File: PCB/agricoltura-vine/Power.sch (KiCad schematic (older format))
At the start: 20 parts, among them T16 1757242, U4 AP63203WU-7, U5 AP63205WU-7

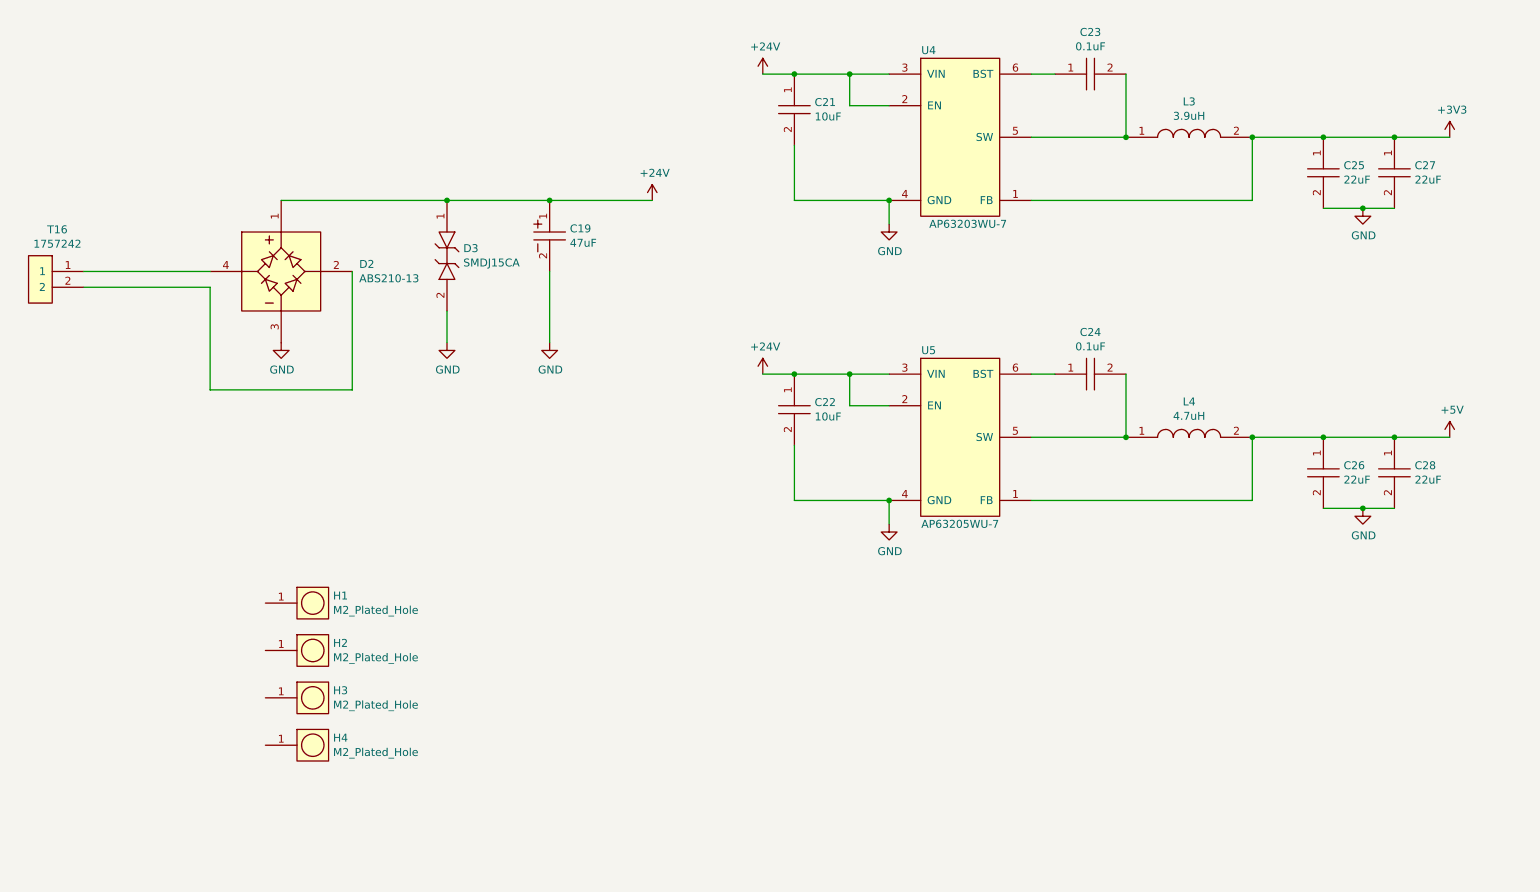
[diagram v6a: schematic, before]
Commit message: Routing and New RS485
swapped over the RS485 chip to a new one and started routing the board.
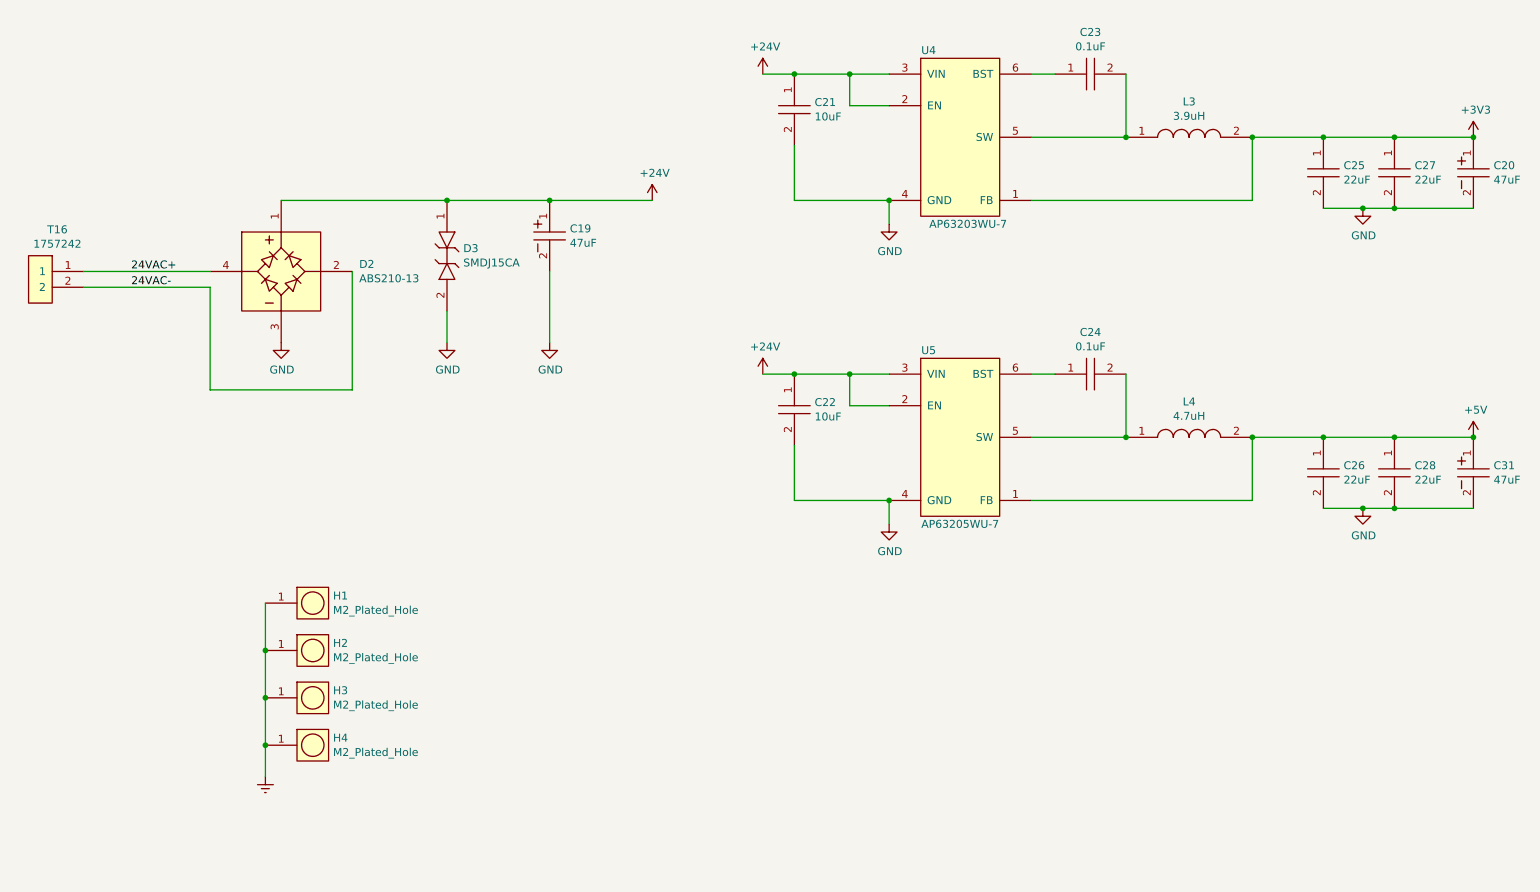
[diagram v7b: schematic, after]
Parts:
- added C20, C31: UCM1C470MCL1GS, AVR-KiCAD-Lib-Capacitors:UCM1C470MCL1GS, symbol AVR-KiCAD-Lib-Capacitors:UCM1C470MCL1GS
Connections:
- net +3V3: now also C20.1
- net +5V: now also C31.1
- net GND: now also C20.2, C31.2
- net 24VAC-: now reaches D2.2, T16.2
- net 24VAC+: now reaches D2.4, T16.1
- net Earth: now reaches H1.1
- net Earth: now also H2.1, H3.1, H4.1

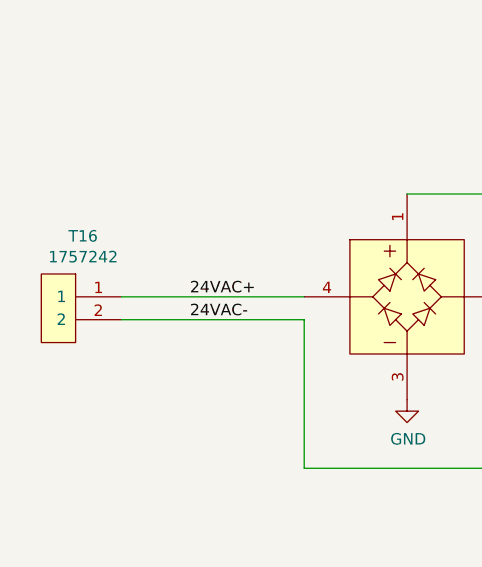
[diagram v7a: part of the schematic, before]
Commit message: IO Expander
added IO expander for 5V IOs
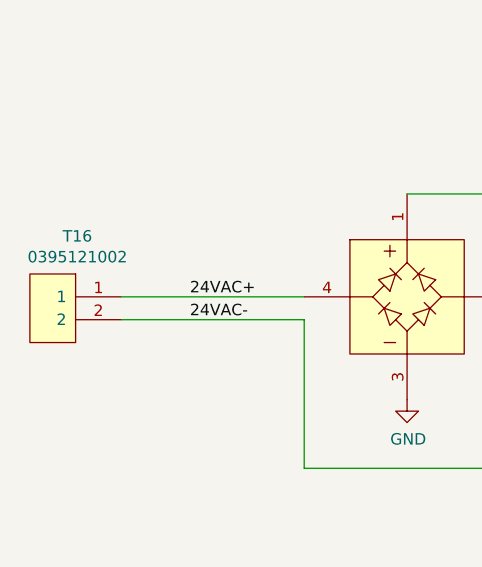
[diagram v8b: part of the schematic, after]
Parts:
- removed T16: 1757242, AVR-KiCAD-Lib-Connectors:PhoenixContact_MSTBA-G_02x5.08mm_Angled, symbol AVR-KiCAD-Lib-Connectors:1757242
- added T16: 0395121002, AVR-KiCAD-Lib-Connectors:0395121002, symbol AVR-KiCAD-Lib-Connectors:0395121002
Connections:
- net 24VAC+: now also T16.1
- net 24VAC-: now also T16.2
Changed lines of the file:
@@
 	1    0    0    -1
-$EndComp
-$Comp
-L AVR-KiCAD-Lib-Connectors:1757242 T16
-U 1 1 5EF359F8
-P 1200 3300
-F 0 "T16" H 1167 3365 50  0000 C CNN
-F 1 "1757242" H 1167 3274 50  0000 C CNN
-F 2 "AVR-KiCAD-Lib-Connectors:PhoenixContact_MSTBA-G_02x5.08mm_Angled" H 1000 3300 50  0001 C CNN
-F 3 "https://media.digikey.com/pdf/Data%20Sheets/Phoenix%20Contact%20PDFs/1757242.pdf" H 1100 3400 50  0001 C CNN
-F 4 "0.64000" H 1300 3550 50  0001 C CNN "Cost QTY: 1"
-F 5 "0.45518" H 1400 3650 50  0001 C CNN "Cost QTY: 1000"
-F 6 "0.43375" H 1500 3750 50  0001 C CNN "Cost QTY: 2500"
-F 7 "0.40698" H 1600 3850 50  0001 C CNN "Cost QTY: 5000"
-F 8 "*" H 1700 3950 50  0001 C CNN "Cost QTY: 10000"
-F 9 "Phoenix Contact" H 1800 4050 50  0001 C CNN "MFR"
-F 10 "1757242" H 1900 4150 50  0001 C CNN "MFR#"
-F 11 "Digikey" H 2000 4250 50  0001 C CNN "Vendor"
-F 12 "277-1106-ND" H 2100 4350 50  0001 C CNN "Vendor #"
-F 13 "AVR" H 2200 4450 50  0001 C CNN "Designer"
-F 14 "12mm" H 2300 4550 50  0001 C CNN "Height"
-F 15 "6/20/2020" H 3400 5650 50  0001 C CNN "Date Created"
-F 16 "6/20/2020" H 2400 4650 50  0001 C CNN "Date Modified"
-F 17 "Yes" H 2500 4750 50  0001 C CNN "Lead-Free ?"
-F 18 "1" H 2600 4850 50  0001 C CNN "RoHS Levels"
-F 19 "ThroughHole" H 2700 4950 50  0001 C CNN "Mounting"
-F 20 "2" H 2800 5050 50  0001 C CNN "Pin Count #"
-F 21 "Active" H 2900 5150 50  0001 C CNN "Status"
-F 22 "*" H 3000 5250 50  0001 C CNN "Tolerance"
-F 23 "Connector" H 3100 5350 50  0001 C CNN "Type"
-F 24 "300V" H 3200 5450 50  0001 C CNN "Voltage"
-F 25 "*" H 3300 5600 50  0001 C CNN "Package"
-F 26 "2 Position Terminal Block Header, Male Pins, Shrouded (4 Side) 0.200\" (5.08mm) 90°, Right Angle  Through Hole" H 3700 6000 50  0001 C CNN "Description"
-F 27 "1757242" H 3500 5800 50  0001 C CNN "_Value_"
-F 28 "*" H 3600 5900 50  0001 C CNN "Management_ID"
-	1    1200 3300
-	-1   0    0    -1
 $EndComp
 Wire Wire Line
@@
 	9700 3100 10200 3100
 Connection ~ 9700 3100
+$Comp
+L AVR-KiCAD-Lib-Connectors:0395121002 T16
+U 1 1 5F06CA83
+P 1200 3500
+F 0 "T16" H 1192 3765 50  0000 C CNN
+F 1 "0395121002" H 1192 3674 50  0000 C CNN
+F 2 "AVR-KiCAD-Lib-Connectors:0395121002" H 250 4550 50  0001 C CNN
+F 3 "https://www.molex.com/pdm_docs/sd/395121002_sd.pdf" H 1100 3600 50  0001 C CNN
+F 4 "0.90000" H 1300 3750 50  0001 C CNN "Cost QTY: 1"
+F 5 "0.30600" H 1400 3850 50  0001 C CNN "Cost QTY: 1000"
+F 6 "*" H 1500 3950 50  0001 C CNN "Cost QTY: 2500"
+F 7 "0.23940" H 1600 4050 50  0001 C CNN "Cost QTY: 5000"
+F 8 "*" H 1700 4150 50  0001 C CNN "Cost QTY: 10000"
+F 9 "Molex" H 1800 4250 50  0001 C CNN "MFR"
+F 10 "0395121002" H 1900 4350 50  0001 C CNN "MFR#"
+F 11 "Digikey" H 2000 4450 50  0001 C CNN "Vendor"
+F 12 "WM23198-ND" H 2100 4550 50  0001 C CNN "Vendor #"
+F 13 "AVR" H 2200 4650 50  0001 C CNN "Designer"
+F 14 "6.86mm" H 2300 4750 50  0001 C CNN "Height"
+F 15 "6/23/2020" H 3400 5850 50  0001 C CNN "Date Created"
+F 16 "6/23/2020" H 2400 4850 50  0001 C CNN "Date Modified"
+F 17 "Yes" H 2500 4950 50  0001 C CNN "Lead-Free ?"
+F 18 "1" H 2600 5050 50  0001 C CNN "RoHS Levels"
+F 19 "ThroughHole" H 2700 5150 50  0001 C CNN "Mounting"
+F 20 "2" H 2800 5250 50  0001 C CNN "Pin Count #"
+F 21 "Active" H 2900 5350 50  0001 C CNN "Status"
+F 22 "*" H 3000 5450 50  0001 C CNN "Tolerance"
+F 23 "Connector" H 3100 5550 50  0001 C CNN "Type"
+F 24 "300V" H 3200 5650 50  0001 C CNN "Voltage"
+F 25 "*" H 3300 5800 50  0001 C CNN "Package"
+F 26 "2 Position Terminal Block Header, Male Pins, Shrouded (4 Side) 0.150\" (3.81mm) 90°, Right Angle  Through Hole" H 3700 6200 50  0001 C CNN "Description"
+F 27 "0395121002" H 3500 6000 50  0001 C CNN "_Value_"
+F 28 "*" H 3600 6100 50  0001 C CNN "Management_ID"
+	1    1200 3500
+	-1   0    0    -1
+$EndComp
 $EndSCHEMATC
